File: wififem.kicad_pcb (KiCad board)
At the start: 2 copper layers, 40 x 48.3 mm, 44 parts, among them J1 Conn_Coaxial, J2 Conn_Coaxial, J3 Conn_Coaxial, J4 Conn_01x05, U1 MCP6566, U2 74HCT04, U3 SE2611T, U4 AP1117-15

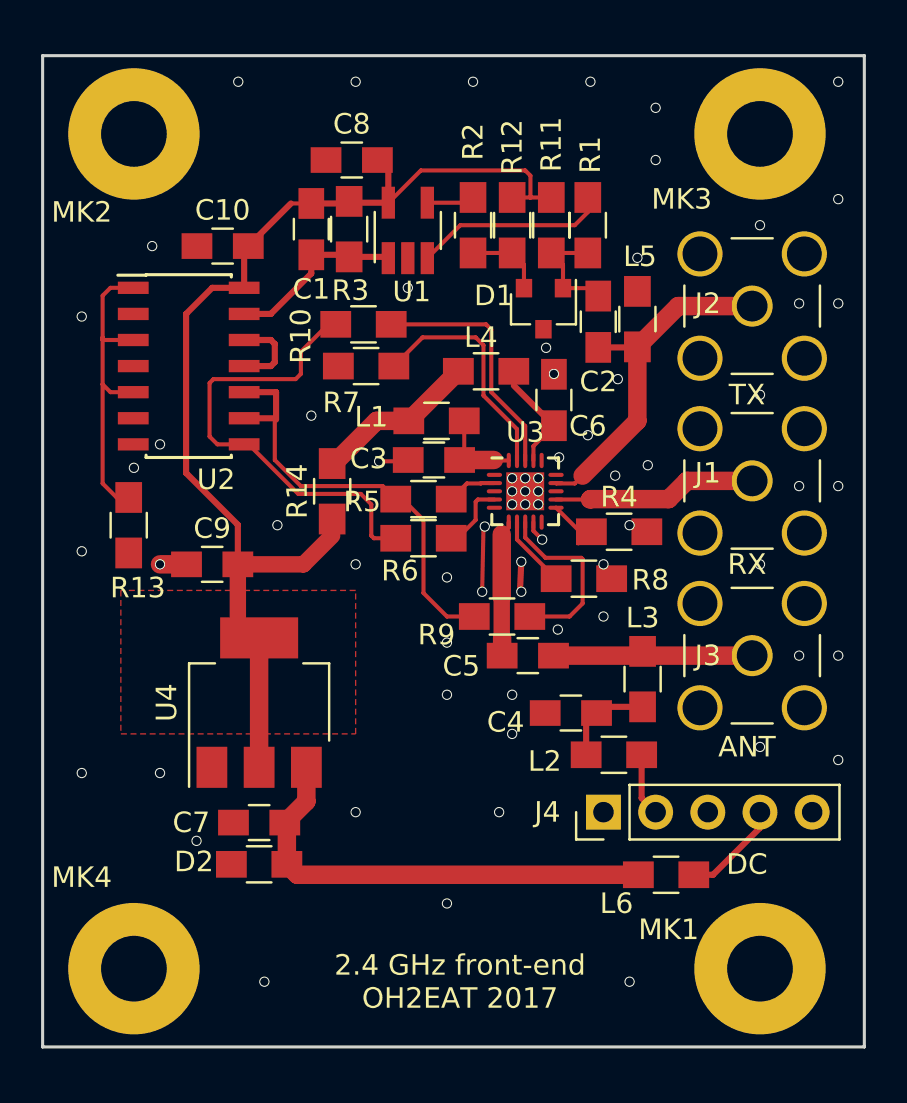
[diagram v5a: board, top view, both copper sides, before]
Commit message: Added missing ground pin in FEM
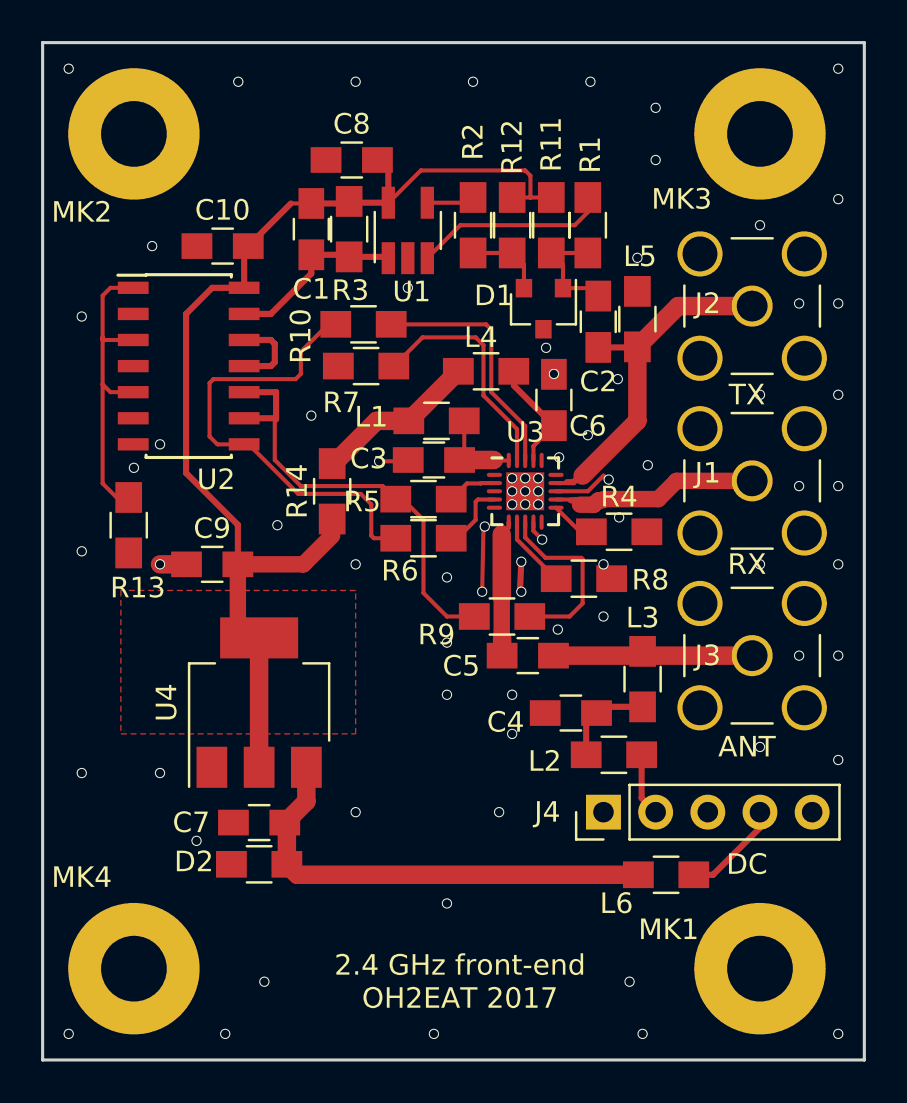
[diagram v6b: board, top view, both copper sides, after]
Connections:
- U3 pad 13: (no net) -> GND
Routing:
- net GND: track 8.45 -> 11.4 mm, vias 69 -> 77
- net Net-(J1-Pad1): track 9.93 -> 10.4 mm
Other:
- board size 40 x 48.3 mm -> 40 x 49.5 mm

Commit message: Add stub
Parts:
- moved C5 2.16 mm to (112.1, 73.4)
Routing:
- net Net-(C5-Pad2): track 7.05 -> 33.3 mm
- net Net-(C5-Pad1): track 9.55 -> 7.81 mm
- net Net-(C2-Pad1): track 5.60 -> 6.58 mm
- net GND: vias 77 -> 115

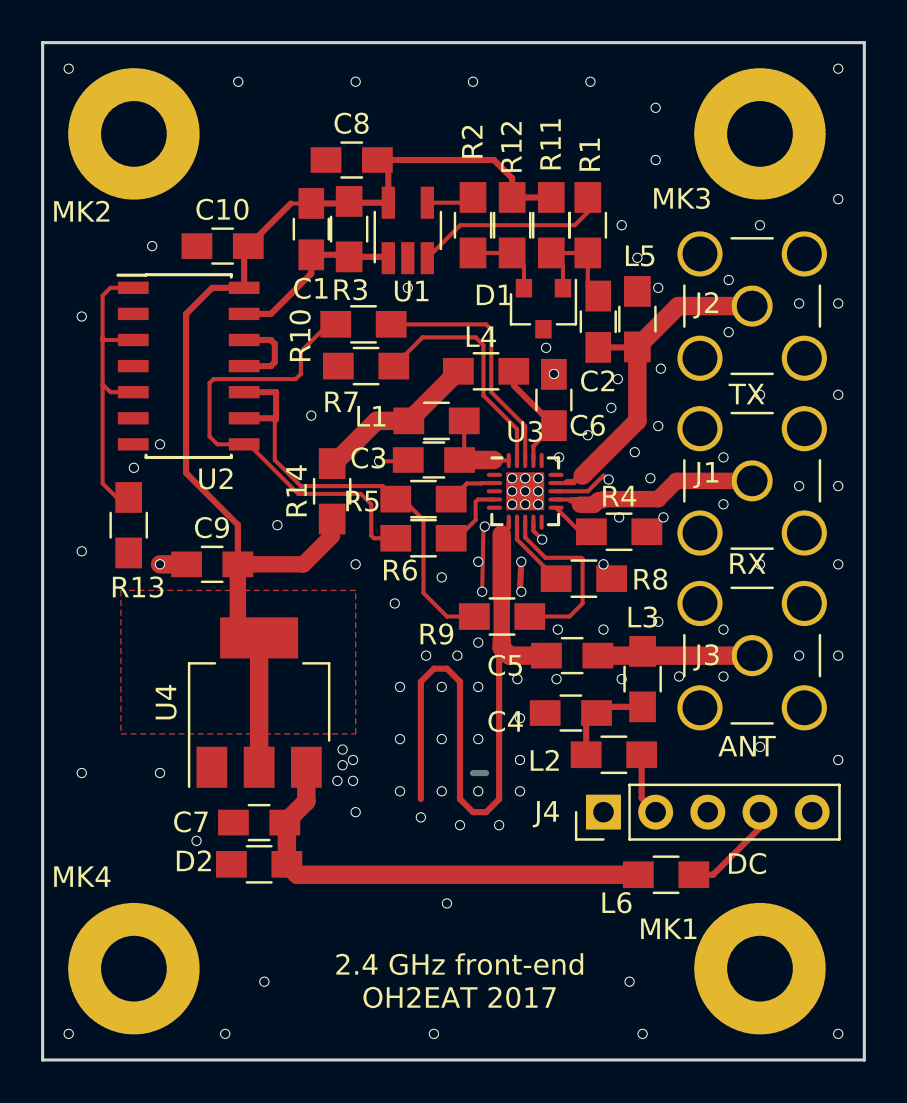
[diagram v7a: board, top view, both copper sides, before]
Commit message: Changed connector placement
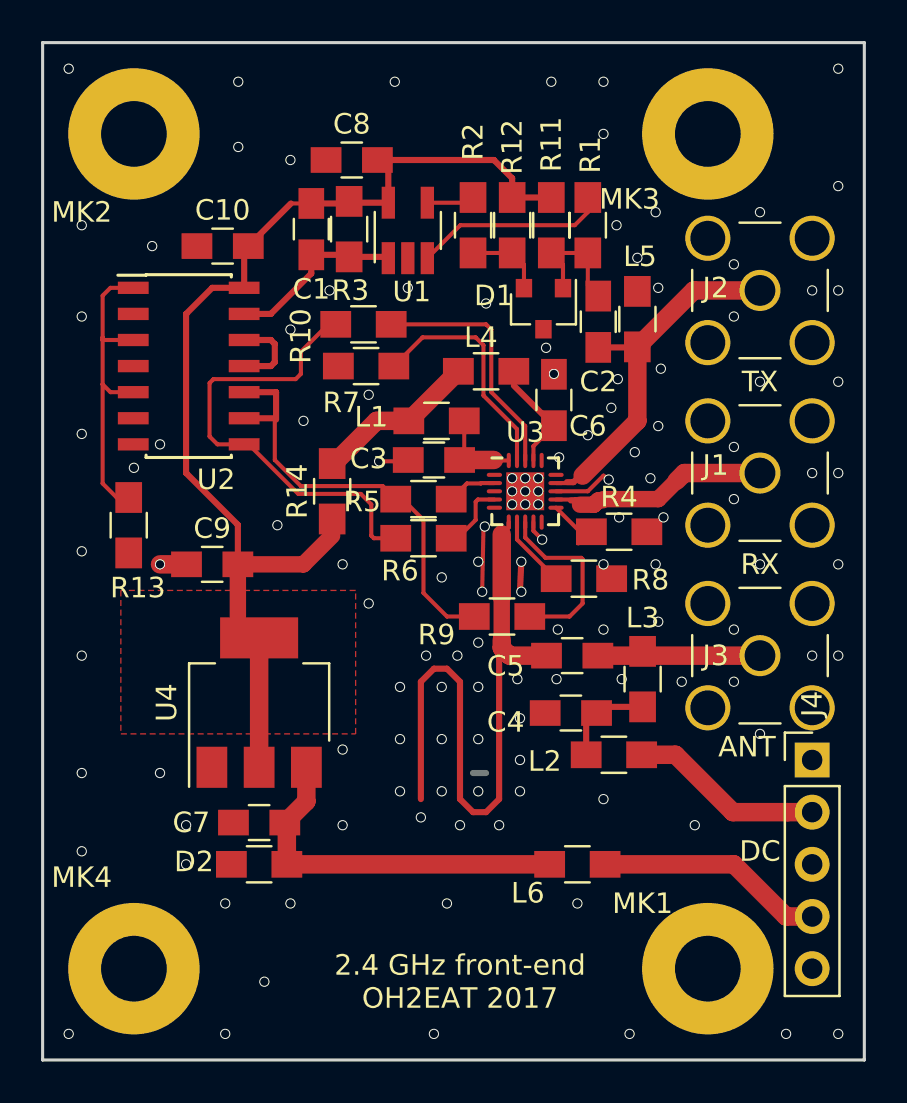
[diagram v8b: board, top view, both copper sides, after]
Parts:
- moved J4 10.5 mm to (123.8, 78.5), turned to 0 degrees
- moved L6 4.35 mm to (112.4, 83.6)
- moved MK1 2.54 mm to (118.7, 88.6)
- moved MK3 2.54 mm to (118.7, 48.0)
- moved J2 0.85 mm to (121.3, 55.6)
- moved J1 0.54 mm to (121.3, 64.5)
- moved J3 0.38 mm to (121.3, 73.4)
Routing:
- net Net-(J4-Pad2): track 3.08 -> 9.46 mm
- net Net-(J4-Pad4): track 4.93 -> 11.1 mm
- net Net-(C7-Pad2): track 22.5 -> 18.0 mm
- net Net-(C2-Pad2): track 17.1 -> 17.8 mm
- net Net-(J1-Pad1): track 10.4 -> 11.0 mm
- net GND: vias 115 -> 127
